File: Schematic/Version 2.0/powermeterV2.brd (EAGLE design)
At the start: 69 x 57 mm, 76 parts, among them K2 RT314F03, Q1 S8050, Q2 S8050, Q3 S8050, Q4 S8050, Y1 16MHz, Y2 NX2012SA-32.768K-STD-MUB-1

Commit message: new firmware with RTC support, PSRAM, new schematic/board with error LED, I2C pullups etc, diodes
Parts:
- added D1, D2: 1N4148, Seeed-OPL-Diode:LL-34
- added ERROR: RED, led:CHIP-LED0805
- added R15: 4.7k, resistor:R0603
- added R29: 10k, resistor:R0603
- added R31: 220, resistor:R0603
- R14, R28: device resistor:R0402 -> resistor:R0603
- R25: value 220 -> 4.7k; device resistor:R0402 -> resistor:R0603
- R26, R27: value 10k -> 1.8k
- moved R14 18.2 mm to (55.6, 38.6), turned to 180 degrees
- moved C28 13.9 mm to (50.3, 30.3), turned to 90 degrees
- moved R25 11.2 mm to (54.9, 16.5), flipped to the top, turned to 270 degrees
- moved C1 2.26 mm to (59.4, 40.0), turned to 0 degrees
- moved R13 1.47 mm to (59.4, 38.6), turned to 180 degrees
- moved R28 0.38 mm to (49.4, 39.5)
- moved RTC 0.23 mm to (56.4, 28.2), turned to 180 degrees
- renumbered K2 to RELAY
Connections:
- net N$45 renamed I34
- removed net N$18: R25.1, RELAY.A3
- removed net N$26: R14.2, RTC.4
- removed net N$32: ESP32.16
- removed net N$46: ESP32.7
- new net DS3231_32KHZ: ESP32.7, R29.1, RTC.1
- new net ERROR_LED: ESP32.16, R31.1
- new net N$16: ERROR.A, R31.2
- net +3V3: now also D1.C, D2.C, R15.2, R29.2, RELAY.A3
- net GND: now also ERROR.C
- net IO32: now also R14.2, RTC.4
- net N$17: now also D1.A
- net N$28: now also D2.A
- net SCL: now also R15.1
- net SDA: now also R25.1
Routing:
- net +3V3: track 146.1 -> 181.0 mm, vias 6 -> 7
- net SDA: track 22.7 -> 6.44 mm
- net DS3231_32KHZ: track 0.00 -> 12.2 mm, vias 0 -> 1
- net DS3231_INT: track 22.5 -> 10.4 mm
- net IO32: track 4.16 -> 14.9 mm, vias 0 -> 1
- net ERROR_LED: track 0.00 -> 7.08 mm
- net GND: track 229.4 -> 222.7 mm, vias 30 -> 34
- net N$28: track 3.57 -> 7.78 mm
- net N$17: track 3.61 -> 7.56 mm
- net N$18: track 3.78 -> 0.00 mm
- net IO0: track 38.6 -> 35.5 mm
- net N$26: track 3.10 -> 0.00 mm
- net SCL: track 14.8 -> 12.7 mm
- net N$16: track 0.00 -> 2.05 mm
- net N$3: track 25.6 -> 26.3 mm

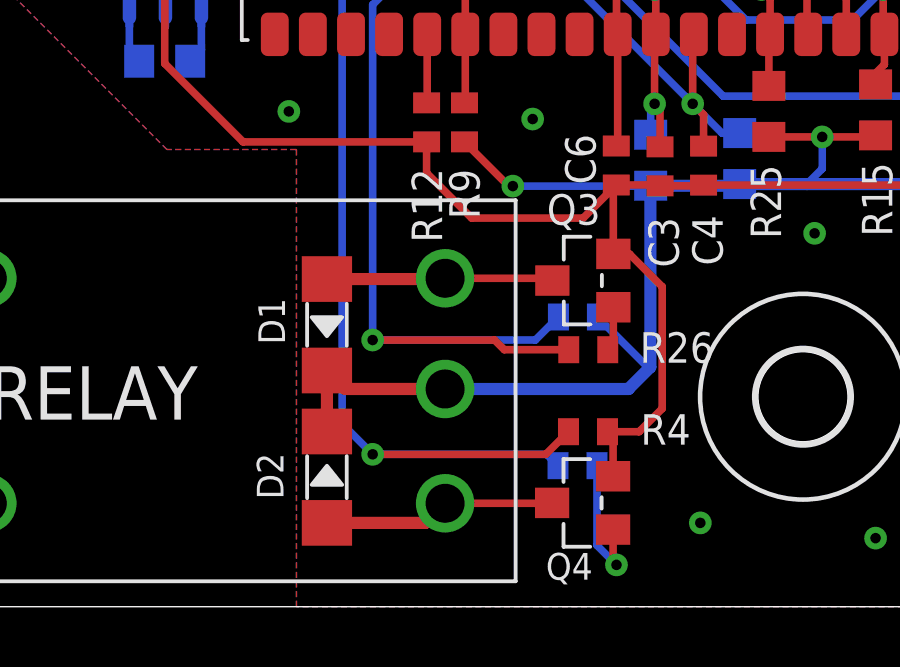
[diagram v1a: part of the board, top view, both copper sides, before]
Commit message: objectify + added logger, timehandler
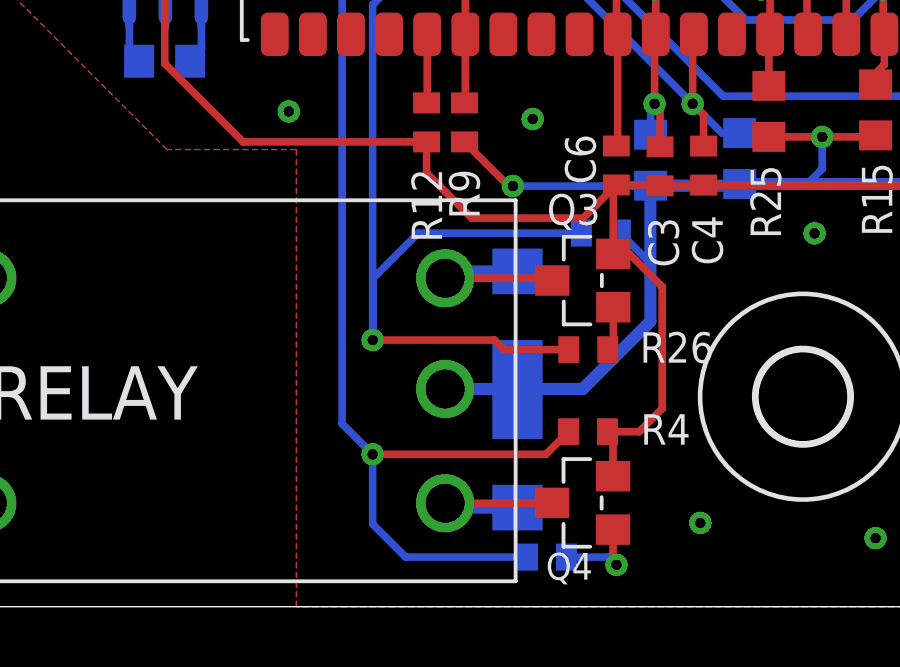
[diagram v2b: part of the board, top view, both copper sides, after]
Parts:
- moved D2 6.37 mm to (46.5, 4.83), flipped to the bottom
- moved D1 6.36 mm to (46.5, 9.65), flipped to the bottom
- moved R27 3.21 mm to (47.5, 1.65)
- moved R5 2.90 mm to (49.3, 12.5)
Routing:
- net +3V3: track 181.0 -> 175.5 mm
- net RELAY_RESET: track 43.3 -> 46.4 mm
- net N$27: track 4.80 -> 3.00 mm
- net N$28: track 7.78 -> 6.06 mm
- net RELAY_SET: track 49.6 -> 51.2 mm
- net N$17: track 7.56 -> 6.15 mm

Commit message: Version renumbering. Hardware Version 1 will now work with Software Version and Hardware Version 2 requires Software Version >= 2
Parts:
- C1: value 1nF -> 100nF
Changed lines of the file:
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@@
 <?xml version="1.0" encoding="utf-8"?>
 <!DOCTYPE eagle SYSTEM "eagle.dtd">
-<eagle version="9.5.0">
+<eagle version="8.4.3">
 <drawing>
 <settings>
@@
 <param name="checkRestrict" value="1"/>
 <param name="checkStop" value="0"/>
-<param name="checkValues" value="0"/>
-<param name="checkNames" value="1"/>
-<param name="checkWireStubs" value="1"/>
-<param name="checkPolygonWidth" value="0"/>
 <param name="useDiameter" value="13"/>
 <param name="maxErrors" value="50"/>
@@
 <attribute name="VALUE" x="35.6052" y="36.35888125" size="1.272840625" layer="27" rot="R270"/>
 </element>
-<element name="C1" library="rcl" library_urn="urn:adsk.eagle:library:334" package="C0402" package3d_urn="urn:adsk.eagle:package:23626/2" value="1nF" x="59.3982" y="39.9854" smashed="yes">
+<element name="C1" library="rcl" library_urn="urn:adsk.eagle:library:334" package="C0402" package3d_urn="urn:adsk.eagle:package:23626/2" value="100nF" x="59.3982" y="39.9854" smashed="yes">
 <attribute name="NAME" x="60.8714" y="39.4774" size="1.016" layer="25"/>
 <attribute name="POPULARITY" value="18" x="59.3982" y="39.9854" size="1.778" layer="27" display="off"/>
@@
 </signal>
 </signals>
-<mfgpreviewcolors>
-<mfgpreviewcolor name="soldermaskcolor" color="0xC8008000"/>
-<mfgpreviewcolor name="silkscreencolor" color="0xFFFEFEFE"/>
-<mfgpreviewcolor name="backgroundcolor" color="0xFF282828"/>
-<mfgpreviewcolor name="coppercolor" color="0xFFFFBF00"/>
-<mfgpreviewcolor name="substratecolor" color="0xFF786E46"/>
-</mfgpreviewcolors>
 <errors>
 </errors>
